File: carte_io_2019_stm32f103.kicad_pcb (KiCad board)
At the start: 2 copper layers, 25 parts, among them J1 Connecteur gauche, J10 capteur_couleur_S, J11 Tirette, J3 Alim logique, J4 Connecteur droit, J8 Liaison serie, J9 capteur_couleur_alim, Q1 PMF370XN, Q3 PMF370XN, Q4 PMF370XN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

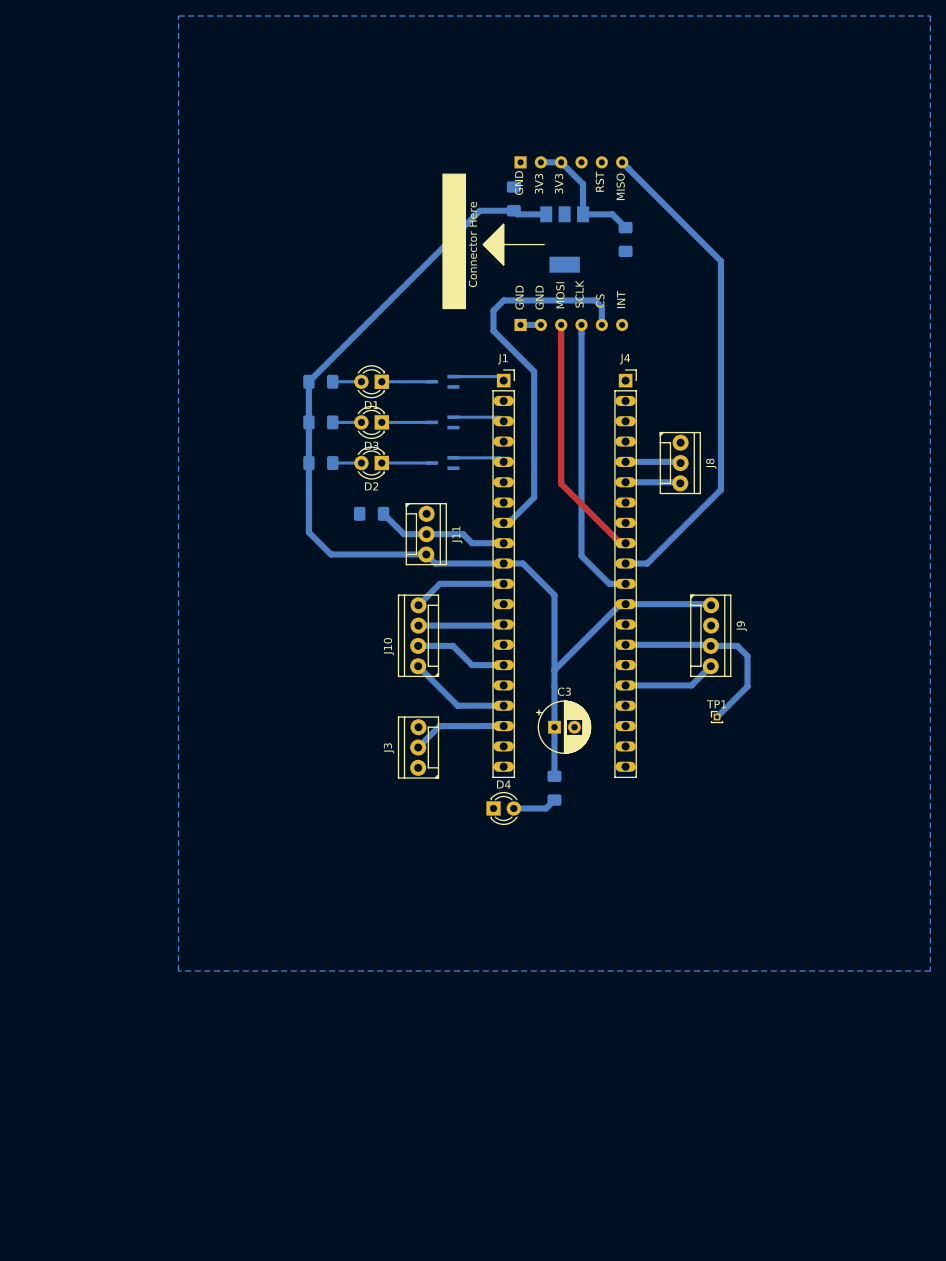
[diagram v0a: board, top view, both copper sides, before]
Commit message: Ajout des capteurs de fin de course
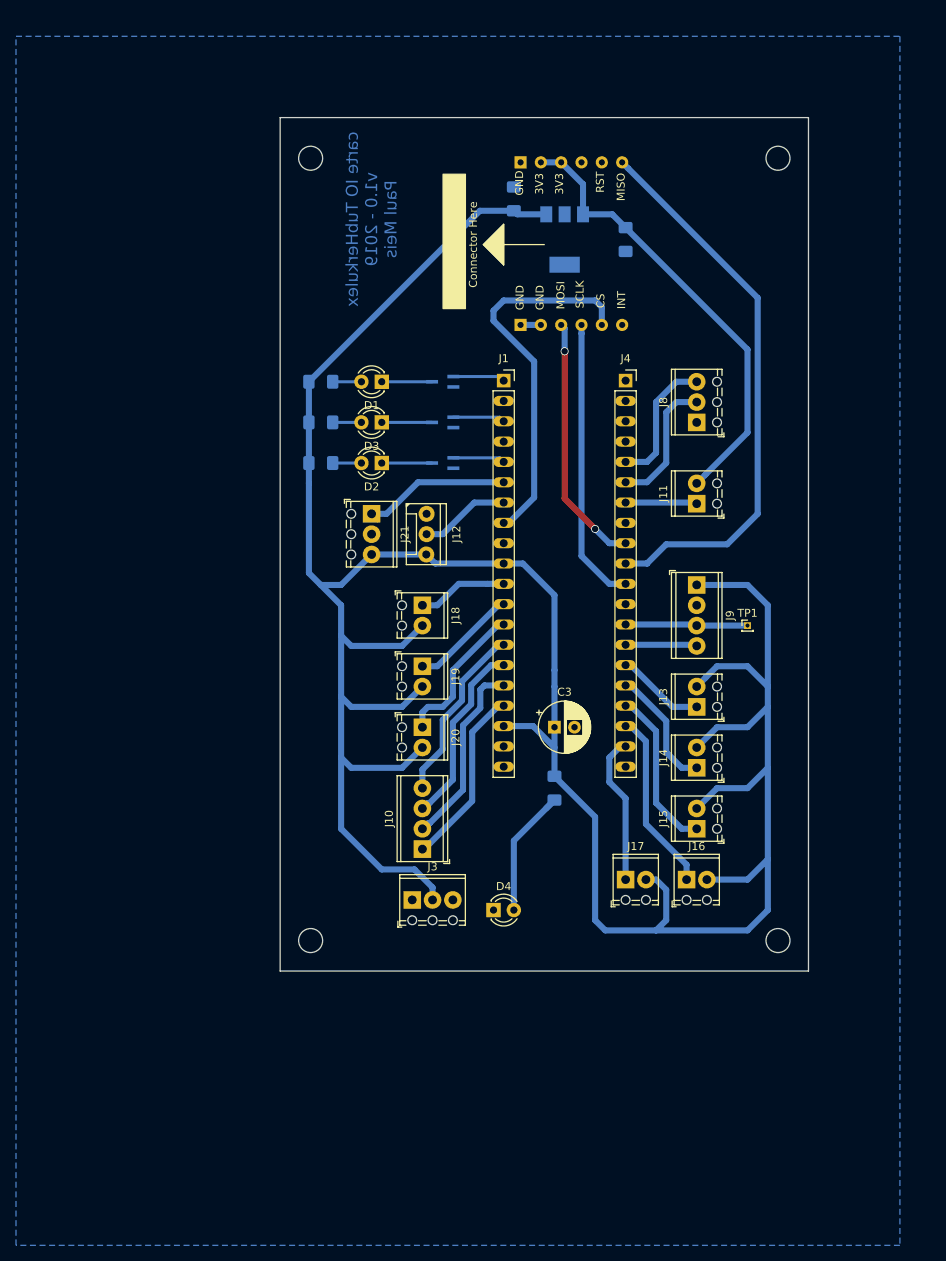
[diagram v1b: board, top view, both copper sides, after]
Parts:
- removed R7: 10k, Resistor_SMD:R_1206_3216Metric_Pad1.42x1.75mm_HandSolder
- added J12: Buzzer, @Robot:HE14-3-straight, F.Cu at (108.0, 95.2)
- added J13: FinCourse1, TerminalBlock_Phoenix:TerminalBlock_Phoenix_MPT-0,5-2-2.54_1x02_P2.54mm_Horizontal, F.Cu at (141.0, 116.8)
- added J14: FinCourse2, TerminalBlock_Phoenix:TerminalBlock_Phoenix_MPT-0,5-2-2.54_1x02_P2.54mm_Horizontal, F.Cu at (141.0, 124.5)
- added J15: FinCourse3, TerminalBlock_Phoenix:TerminalBlock_Phoenix_MPT-0,5-2-2.54_1x02_P2.54mm_Horizontal, F.Cu at (141.0, 132.1)
- added J16: FinCourse4, TerminalBlock_Phoenix:TerminalBlock_Phoenix_MPT-0,5-2-2.54_1x02_P2.54mm_Horizontal, F.Cu at (139.7, 138.4)
- added J17: FinCourse5, TerminalBlock_Phoenix:TerminalBlock_Phoenix_MPT-0,5-2-2.54_1x02_P2.54mm_Horizontal, F.Cu at (132.1, 138.4)
- added J18: FinCourse6, TerminalBlock_Phoenix:TerminalBlock_Phoenix_MPT-0,5-2-2.54_1x02_P2.54mm_Horizontal, F.Cu at (106.7, 104.1)
- added J19: FinCourse7, TerminalBlock_Phoenix:TerminalBlock_Phoenix_MPT-0,5-2-2.54_1x02_P2.54mm_Horizontal, F.Cu at (106.7, 111.8)
- added J20: FinCourse8, TerminalBlock_Phoenix:TerminalBlock_Phoenix_MPT-0,5-2-2.54_1x02_P2.54mm_Horizontal, F.Cu at (106.7, 119.4)
- added J21: Piston, TerminalBlock_Phoenix:TerminalBlock_Phoenix_MPT-0,5-3-2.54_1x03_P2.54mm_Horizontal, F.Cu at (100.3, 92.7)
- J10, J9: footprint @Robot:HE14-4-straight -> TerminalBlock_Phoenix:TerminalBlock_Phoenix_MPT-0,5-4-2.54_1x04_P2.54mm_Horizontal
- J11: footprint @Robot:HE14-3-straight -> TerminalBlock_Phoenix:TerminalBlock_Phoenix_MPT-0,5-2-2.54_1x02_P2.54mm_Horizontal
- J3, J8: footprint @Robot:HE14-3-straight -> TerminalBlock_Phoenix:TerminalBlock_Phoenix_MPT-0,5-3-2.54_1x03_P2.54mm_Horizontal
- moved J11 33.2 mm to (141.0, 91.4), turned to 90 degrees
- moved J10 25.4 mm to (106.7, 134.6)
- moved J3 19.0 mm to (105.4, 141.0), turned to 0 degrees
- moved D4 12.7 mm to (115.6, 142.2)
- moved TP1 12.0 mm to (147.3, 106.7)
- moved J9 5.68 mm to (141.0, 101.6)
- moved J8 5.24 mm to (141.0, 81.3), turned to 90 degrees
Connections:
- J1 pad 11: /S3 -> /fin_course_6
- J1 pad 12: Net-(J1-Pad12) -> /fin_course_7
- J1 pad 13: /S2 -> /fin_course_8
- J1 pad 14: Net-(J1-Pad14) -> /S3
- J1 pad 15: /S1 -> /S2
- J1 pad 16: Net-(J1-Pad16) -> /S1
- J1 pad 2: Net-(J1-Pad2) -> GND
- J1 pad 6: Net-(J1-Pad6) -> /piston
- J1 pad 7: Net-(J1-Pad7) -> /buzzer
- J1 pad 9: /out_tirette -> Net-(J1-Pad9)
- J11 pad 1: GND -> /out_tirette
- J11 pad 2: /out_tirette -> +3V3
- J4 pad 12: +5V -> GND
- J4 pad 13: Net-(J4-Pad13) -> /out_couleur
- J4 pad 14: /out_couleur -> /LED_couleur
- J4 pad 15: Net-(J4-Pad15) -> /fin_course_1
- J4 pad 16: /LED_couleur -> /fin_course_2
- J4 pad 17: Net-(J4-Pad17) -> /fin_course_3
- J4 pad 18: Net-(J4-Pad18) -> /fin_course_4
- J4 pad 19: Net-(J4-Pad19) -> /fin_course_5
- J4 pad 7: Net-(J4-Pad7) -> /out_tirette
- J8 pad 2: /RX -> /TX
- J8 pad 3: /TX -> /RX
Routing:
- net +5V: track 149.0 -> 352.1 mm
- net +3V3: track 16.2 -> 57.1 mm
- net /fin_course_4: track 0.00 -> 22.7 mm
- net /fin_course_3: track 0.00 -> 20.5 mm
- net /piston: track 0.00 -> 19.1 mm
- net /fin_course_8: track 0.00 -> 18.7 mm
- net /fin_course_5: track 0.00 -> 18.7 mm
- net /fin_course_2: track 0.00 -> 15.4 mm
- net /fin_course_7: track 0.00 -> 13.4 mm
- net /S1: track 11.7 -> 24.3 mm
- net /S2: track 10.7 -> 23.2 mm
- net /buzzer: track 0.00 -> 11.9 mm
- net Net-(D4-Pad2): track 5.52 -> 17.3 mm
- net /fin_course_6: track 0.00 -> 11.3 mm
- net /fin_course_1: track 0.00 -> 11.1 mm
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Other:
- board outline added: 66 x 106.7 mm
- board text added: "carte IO TubHerkulex v1.0 - 2019 Paul Meis"

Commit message: Fix buzzer
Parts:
- moved J12 2.54 mm to (110.5, 95.2)
- moved J21 2.54 mm to (97.8, 92.7)
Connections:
- J1 pad 9: Net-(J1-Pad9) -> GND
- J12 pad 1: GND -> /buzzer
- J12 pad 2: /buzzer -> GND
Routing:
- net /buzzer: track 11.9 -> 8.31 mm
- net /piston: track 19.1 -> 20.7 mm
- net +5V: track 352.1 -> 353.6 mm
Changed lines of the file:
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@@
     (zones 0)
     (modules 34)
-    (nets 47)
+    (nets 46)
   )
   (page A4)
@@
   (net 44 /fin_course_1)
   (net 45 /piston)
-  (net 46 "Net-(J1-Pad9)")
   (net_class Default "Ceci est la Netclass par défaut."
     (clearance 0.381)
@@
     (add_net "Net-(J1-Pad20)")
     (add_net "Net-(J1-Pad4)")
-    (add_net "Net-(J1-Pad9)")
     (add_net "Net-(J3-Pad3)")
     (add_net "Net-(J4-Pad20)")
@@
   )
   (module TerminalBlock_Phoenix:TerminalBlock_Phoenix_MPT-0,5-3-2.54_1x03_P2.54mm_Horizontal (layer F.Cu)
-    (at 100.33 92.71 270)
+    (at 97.79 92.71 270)
     (descr "Terminal Block Phoenix MPT-0,5-3-2.54, 3 pins, pitch 2.54mm, size 8.08x6.2mm^2, drill diamater 1.1mm, pad diameter 2.2mm, see http://www.mouser.com/ds/2/324/ItemDetail_1725656-920552.pdf, script-generated using https://github.com/pointhi/kicad-footprint-generator/scripts/TerminalBlock_Phoenix")
     (tags "THT Terminal Block Phoenix MPT-0,5-3-2.54 pitch 2.54mm size 8.08x6.2mm^2 drill 1.1mm pad 2.2mm")
@@
       (net 1 +5V))
     (pad 9 thru_hole oval (at 0 20.32) (size 2.54 1.27) (drill 1) (layers *.Cu *.Mask)
-      (net 46 "Net-(J1-Pad9)"))
+      (net 2 GND))
     (pad 8 thru_hole oval (at 0 17.78) (size 2.54 1.27) (drill 1) (layers *.Cu *.Mask)
       (net 34 /CS))
@@
   )
   (module @Robot:HE14-3-straight (layer F.Cu)
-    (at 107.95 95.25 270)
+    (at 110.49 95.25 270)
     (tags "HE14 3 straight connector 1x3")
     (fp_text reference J12 (at 0 -3 270) (layer F.SilkS)
@@
     (fp_line (start 3.81 3.283747) (end -3.81 3.283747) (layer F.CrtYd) (width 0.15))
     (pad 1 thru_hole circle (at -2.54 0.743747 90) (size 2 2) (drill 1) (layers *.Cu *.Mask)
+      (net 36 /buzzer))
+    (pad 2 thru_hole circle (at 0 0.743747 90) (size 2 2) (drill 1) (layers *.Cu *.Mask)
       (net 2 GND))
-    (pad 2 thru_hole circle (at 0 0.743747 90) (size 2 2) (drill 1) (layers *.Cu *.Mask)
-      (net 36 /buzzer))
     (pad 3 thru_hole circle (at 2.54 0.783747 90) (size 2 2) (drill 1) (layers *.Cu *.Mask)
       (net 1 +5V))
@@
   (segment (start 122.16 55.27) (end 118.5525 55.27) (width 0.762) (layer B.Cu) (net 1))
   (segment (start 123.19 112.255) (end 123.19 114.3) (width 0.762) (layer B.Cu) (net 1))
-  (segment (start 132.08 104) (end 131.445 104) (width 0.762) (layer B.Cu) (net 2))
   (segment (start 123.19 119.38) (end 123.19 114.3) (width 0.762) (layer B.Cu) (net 1))
   (segment (start 113.865 54.8275) (end 110.055 58.6375) (width 0.762) (layer B.Cu) (net 1))
@@
   (segment (start 147.32 119.38) (end 149.86 116.84) (width 0.762) (layer B.Cu) (net 1))
   (segment (start 149.86 142.24) (end 149.86 116.84) (width 0.762) (layer B.Cu) (net 1))
-  (segment (start 108.296253 98.92) (end 107.166253 97.79) (width 0.762) (layer B.Cu) (net 1))
-  (segment (start 116.84 98.92) (end 108.296253 98.92) (width 0.762) (layer B.Cu) (net 1))
-  (segment (start 107.166253 97.79) (end 100.33 97.79) (width 0.762) (layer B.Cu) (net 1))
   (segment (start 92.4925 88.9) (end 92.4925 86.36) (width 0.762) (layer B.Cu) (net 1))
-  (segment (start 100.33 97.79) (end 96.52 101.6) (width 0.762) (layer B.Cu) (net 1))
-  (segment (start 96.52 101.6) (end 93.98 101.6) (width 0.762) (layer B.Cu) (net 1))
   (segment (start 93.98 101.6) (end 92.4925 100.1125) (width 0.762) (layer B.Cu) (net 1))
   (segment (start 92.4925 100.1125) (end 92.4925 88.9) (width 0.762) (layer B.Cu) (net 1))
@@
   (segment (start 149.86 104.14) (end 149.86 114.3) (width 0.762) (layer B.Cu) (net 1))
   (segment (start 147.32 101.6) (end 149.86 104.14) (width 0.762) (layer B.Cu) (net 1))
-  (segment (start 100.33 92.71) (end 101.007999 93.387999) (width 0.762) (layer B.Cu) (net 45))
+  (segment (start 102.87 97.79) (end 109.706253 97.79) (width 0.762) (layer B.Cu) (net 1))
+  (segment (start 110.836253 98.92) (end 109.706253 97.79) (width 0.762) (layer B.Cu) (net 1))
+  (segment (start 116.84 98.92) (end 110.836253 98.92) (width 0.762) (layer B.Cu) (net 1))
+  (segment (start 102.87 97.79) (end 97.79 97.79) (width 0.762) (layer B.Cu) (net 1))
+  (segment (start 96.52 99.06) (end 97.79 97.79) (width 0.762) (layer B.Cu) (net 1))
+  (segment (start 96.52 104.14) (end 96.52 99.06) (width 0.762) (layer B.Cu) (net 1))
+  (segment (start 132.08 104) (end 131.445 104) (width 0.762) (layer B.Cu) (net 2))
   (segment (start 118.95 69.095) (end 121.49 69.095) (width 0.762) (layer B.Cu) (net 2))
-  (via (at 124.46 72.39) (size 1) (drill 0.8) (layers F.Cu B.Cu) (net 33))
   (segment (start 121.49 48.775) (end 124.03 48.775) (width 0.762) (layer B.Cu) (net 3))
   (segment (start 130.4175 55.27) (end 132.08 56.9325) (width 0.762) (layer B.Cu) (net 3))
@@
   (segment (start 144.78 96.52) (end 148.59 92.71) (width 0.762) (layer B.Cu) (net 32))
   (segment (start 137.16 96.52) (end 144.78 96.52) (width 0.762) (layer B.Cu) (net 32))
+  (via (at 124.46 72.39) (size 1) (drill 0.8) (layers F.Cu B.Cu) (net 33))
   (segment (start 132.08 96.38) (end 131.445 96.38) (width 0.762) (layer B.Cu) (net 33))
   (segment (start 131.445 96.38) (end 132.08 96.38) (width 0.762) (layer F.Cu) (net 33))
@@
   (segment (start 120.65 73.66) (end 115.57 68.58) (width 0.762) (layer B.Cu) (net 34))
   (segment (start 117.475 91.3) (end 116.84 91.3) (width 0.762) (layer B.Cu) (net 36))
-  (segment (start 107.206253 95.25) (end 109.22 95.25) (width 0.762) (layer B.Cu) (net 36))
-  (segment (start 113.17 91.3) (end 116.84 91.3) (width 0.762) (layer B.Cu) (net 36))
-  (segment (start 109.22 95.25) (end 113.17 91.3) (width 0.762) (layer B.Cu) (net 36))
+  (segment (start 111.156253 91.3) (end 116.84 91.3) (width 0.762) (layer B.Cu) (net 36))
+  (segment (start 109.746253 92.71) (end 111.156253 91.3) (width 0.762) (layer B.Cu) (net 36))
   (segment (start 114.808 101.46) (end 116.84 101.46) (width 0.762) (layer B.Cu) (net 37))
   (segment (start 111.222 101.46) (end 114.808 101.46) (width 0.762) (layer B.Cu) (net 37))
@@
   (segment (start 137.935 116.84) (end 132.715 111.62) (width 0.762) (layer B.Cu) (net 44))
   (segment (start 140.97 116.84) (end 137.935 116.84) (width 0.762) (layer B.Cu) (net 44))
-  (segment (start 102.192 92.71) (end 100.33 92.71) (width 0.762) (layer B.Cu) (net 45))
-  (segment (start 106.142 88.76) (end 102.192 92.71) (width 0.762) (layer B.Cu) (net 45))
   (segment (start 116.84 88.76) (end 106.142 88.76) (width 0.762) (layer B.Cu) (net 45))
+  (segment (start 103.602 88.76) (end 106.142 88.76) (width 0.762) (layer B.Cu) (net 45))
+  (segment (start 99.652 92.71) (end 103.602 88.76) (width 0.762) (layer B.Cu) (net 45))
+  (segment (start 97.79 92.71) (end 99.652 92.71) (width 0.762) (layer B.Cu) (net 45))
   (zone (net 2) (net_name GND) (layer B.Cu) (hatch edge 0.508)
     (connect_pads (clearance 0.508))

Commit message: Replacage de led_feedback sur PC13
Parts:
- moved R5 75.1 mm to (132.1, 146.1), turned to 90 degrees
- moved D3 64.8 mm to (132.1, 138.4), turned to 270 degrees
- moved Q4 56.9 mm to (132.1, 133.3), turned to 270 degrees
- moved J17 50.3 mm to (97.8, 101.6), turned to 270 degrees
- moved J18 10.2 mm to (97.8, 109.2)
- moved J19 10.2 mm to (97.8, 116.8)
- moved J20 10.2 mm to (97.8, 124.5)
- moved J10 10.2 mm to (97.8, 139.7)
- moved J3 5.08 mm to (105.4, 146.1)
- moved D2 5.08 mm to (101.6, 81.3)
- moved Q3 5.08 mm to (109.2, 81.3)
- moved R4 5.08 mm to (94.0, 81.3)
- moved D4 5.08 mm to (115.6, 147.3)
- moved J12 2.54 mm to (110.5, 92.7)
- moved J21 2.54 mm to (97.8, 90.2)
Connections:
- J1 pad 10: +5V -> /fin_course_5
- J1 pad 3: /led_feedback -> /led_communication
- J1 pad 5: /led_communication -> /piston
- J1 pad 6: /piston -> /buzzer
- J1 pad 7: /buzzer -> Net-(J1-Pad7)
- J1 pad 9: GND -> +5V
- J4 pad 19: /fin_course_5 -> /led_feedback
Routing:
- net /fin_course_7: track 13.4 -> 27.3 mm
- net /fin_course_8: track 18.7 -> 30.5 mm
- net /fin_course_6: track 11.3 -> 22.3 mm
- net /S3: track 22.5 -> 33.0 mm
- net /S0: track 22.6 -> 33.2 mm
- net /S2: track 23.2 -> 33.7 mm
- net /S1: track 24.3 -> 33.9 mm
- net /led_feedback: track 7.14 -> 15.2 mm
- net Net-(D4-Pad2): track 17.3 -> 22.4 mm
- net Net-(D3-Pad1): track 6.29 -> 3.75 mm
- net +5V: track 353.6 -> 355.3 mm
- net /fin_course_5: track 18.7 -> 20.2 mm
- net /led_communication: track 6.50 -> 7.86 mm
- net Net-(J1-Pad7): track 0.00 -> 0.63 mm
- net /buzzer: track 8.31 -> 7.68 mm
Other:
- board size 66 x 106.7 mm -> 66 x 109.2 mm
